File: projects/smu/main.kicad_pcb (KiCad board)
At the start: 4 copper layers, 94 parts, among them P301 CONN_01X15, P302 CONN_01X03, P401 CONN_01X12, P501 CONN_01X07, Q501 MMBT3904, Q502 MMBT3904, U301 LM741, U302 DG444, U303 LM741, U304 LM741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

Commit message: add nettie library etc
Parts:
- removed C411, C412: C, Capacitors_SMD:C_1206
- removed C501, C503, C506: 10uF, Capacitors_SMD:C_1206
- removed C502: 10p, Capacitors_SMD:C_1206
- removed C504, C505, C507, C508: 0.1uF, Capacitors_SMD:C_1206
- removed P301: CONN_01X15, Pin_Headers:Pin_Header_Straight_1x15
- removed P302: CONN_01X03, Pin_Headers:Pin_Header_Straight_1x03
- removed P401: CONN_01X12, Pin_Headers:Pin_Header_Straight_1x12
- removed P501: CONN_01X07, Pin_Headers:Pin_Header_Straight_1x07
- removed Q501, Q502: MMBT3904, TO_SOT_Packages_SMD:SOT-23
- removed R502: 1M, Resistors_SMD:R_1206
- removed R503: 10k, Resistors_SMD:R_1206
- removed R504: 1k, Resistors_ThroughHole:Resistor_TO-220_Vertical
- removed R505, R508: 10k, Resistors_ThroughHole:Resistor_TO-220_Vertical
- removed R506: 120, Resistors_ThroughHole:Resistor_TO-220_Vertical
- removed R507: 5.1k, Resistors_ThroughHole:Resistor_TO-220_Vertical
- removed R510: R, Resistors_SMD:R_1206
- removed RV501, RV502: 1k, Potentiometers:Potentiometer_Bourns_3296Y_3-8Zoll_Angular_ScrewUp
- removed U403, U406, U407, U501, U502: LM741, Housings_SOIC:SOIC-8_3.9x4.9mm_Pitch1.27mm
- removed U503: 2DW232, footprint:TO-5_Housing_2DW232_5Pin
- added P101: CONN_01X15, Pin_Headers:Pin_Header_Straight_1x15, F.Cu at (35.0, 64.0)
- added P102: CONN_01X34, Pin_Headers:Pin_Header_Straight_1x34, F.Cu at (-22.0, 1.00)
- added R307, R308: R, Resistors_SMD:R_1206, F.Cu at (0.00, 0.00)
- added W401, W402: NET-TIE, footprint:NET-TIE-0.3mm, F.Cu at (0.00, 0.00)
- U402, U404: value LM741 -> LM324; footprint Housings_SOIC:SOIC-8_3.9x4.9mm_Pitch1.27mm -> Housings_SOIC:SOIC-14_3.9x8.7mm_Pitch1.27mm
- U405: value LM741 -> DG444; footprint Housings_SOIC:SOIC-8_3.9x4.9mm_Pitch1.27mm -> Housings_SOIC:SOIC-16_3.9x9.9mm_Pitch1.27mm
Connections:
- R403 pad 1: REFGND -> AGND
- R416 pad 2: REF-CTL -> Net-(R416-Pad2)
- U401 pad 11: (no net) -> AGND
- U401 pad 18: REFGND -> AGND
- U401 pad 2: (no net) -> DAC_CS
- U401 pad 20: REFGND -> AGND
- U401 pad 29: REFGND -> AGND
- U401 pad 3: (no net) -> DAC_SLCK
- U401 pad 32: REFGND -> AGND
- U401 pad 4: (no net) -> DAC_SDI
- U401 pad 41: REFGND -> AGND
- U401 pad 43: REFGND -> AGND
- U401 pad 5: (no net) -> DAC_SDO
- U401 pad 6: (no net) -> DAC_LDAC
- U401 pad 7: (no net) -> DAC_RST
- U402 pad 2: Net-(R404-Pad1) -> AGND
- U402 pad 4: -VE -> +VE
- U402 pad 5: (no net) -> AGND
- U402 pad 6: Net-(R406-Pad1) -> AGND
- U402 pad 7: +VE -> (no net)
- U402 pad 8: (no net) -> Net-(R406-Pad1)
- U404 pad 1: (no net) -> Net-(D401-Pad2)
- U404 pad 4: -VE -> +VE
- U404 pad 5: (no net) -> Net-(R412-Pad1)
- U404 pad 6: Net-(D401-Pad2) -> OUT
- U404 pad 7: +VE -> Net-(D404-Pad1)
- U404 pad 8: (no net) -> Net-(D402-Pad2)
- U405 pad 1: (no net) -> REF_IN1
- U405 pad 2: OUT -> Net-(R416-Pad2)
- U405 pad 3: Net-(R412-Pad1) -> Net-(U405-Pad3)
- U405 pad 5: (no net) -> AGND
- U405 pad 6: Net-(D404-Pad1) -> AGND
- U405 pad 7: +VE -> Net-(R416-Pad2)
- U405 pad 8: (no net) -> REF_IN4
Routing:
- net REF: track 286.8 -> 98.1 mm
- net OUT: track 140.1 -> 0.00 mm, vias 2 -> 0
- net 3.3V: track 132.9 -> 7.72 mm, vias 3 -> 0
- net TRIGGER: track 118.4 -> 3.27 mm
- net H-GND: track 75.1 -> 0.00 mm
- net Net-(Q502-Pad2): track 71.0 -> 0.00 mm
- net REF-CTL: track 68.1 -> 0.00 mm, vias 1 -> 0
- net -VE: track 167.6 -> 100.2 mm, vias 17 -> 14
- net +VE: track 194.9 -> 128.1 mm, vias 21 -> 14
- net AGND: track 234.8 -> 176.9 mm, vias 33 -> 26
- net Net-(Q501-Pad2): track 48.4 -> 0.00 mm
- net I-FB: track 58.1 -> 15.2 mm
- net V-FB: track 53.0 -> 12.4 mm
- net Net-(R307-Pad1): track 35.4 -> 0.18 mm
- net Net-(C502-Pad1): track 33.0 -> 0.00 mm
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
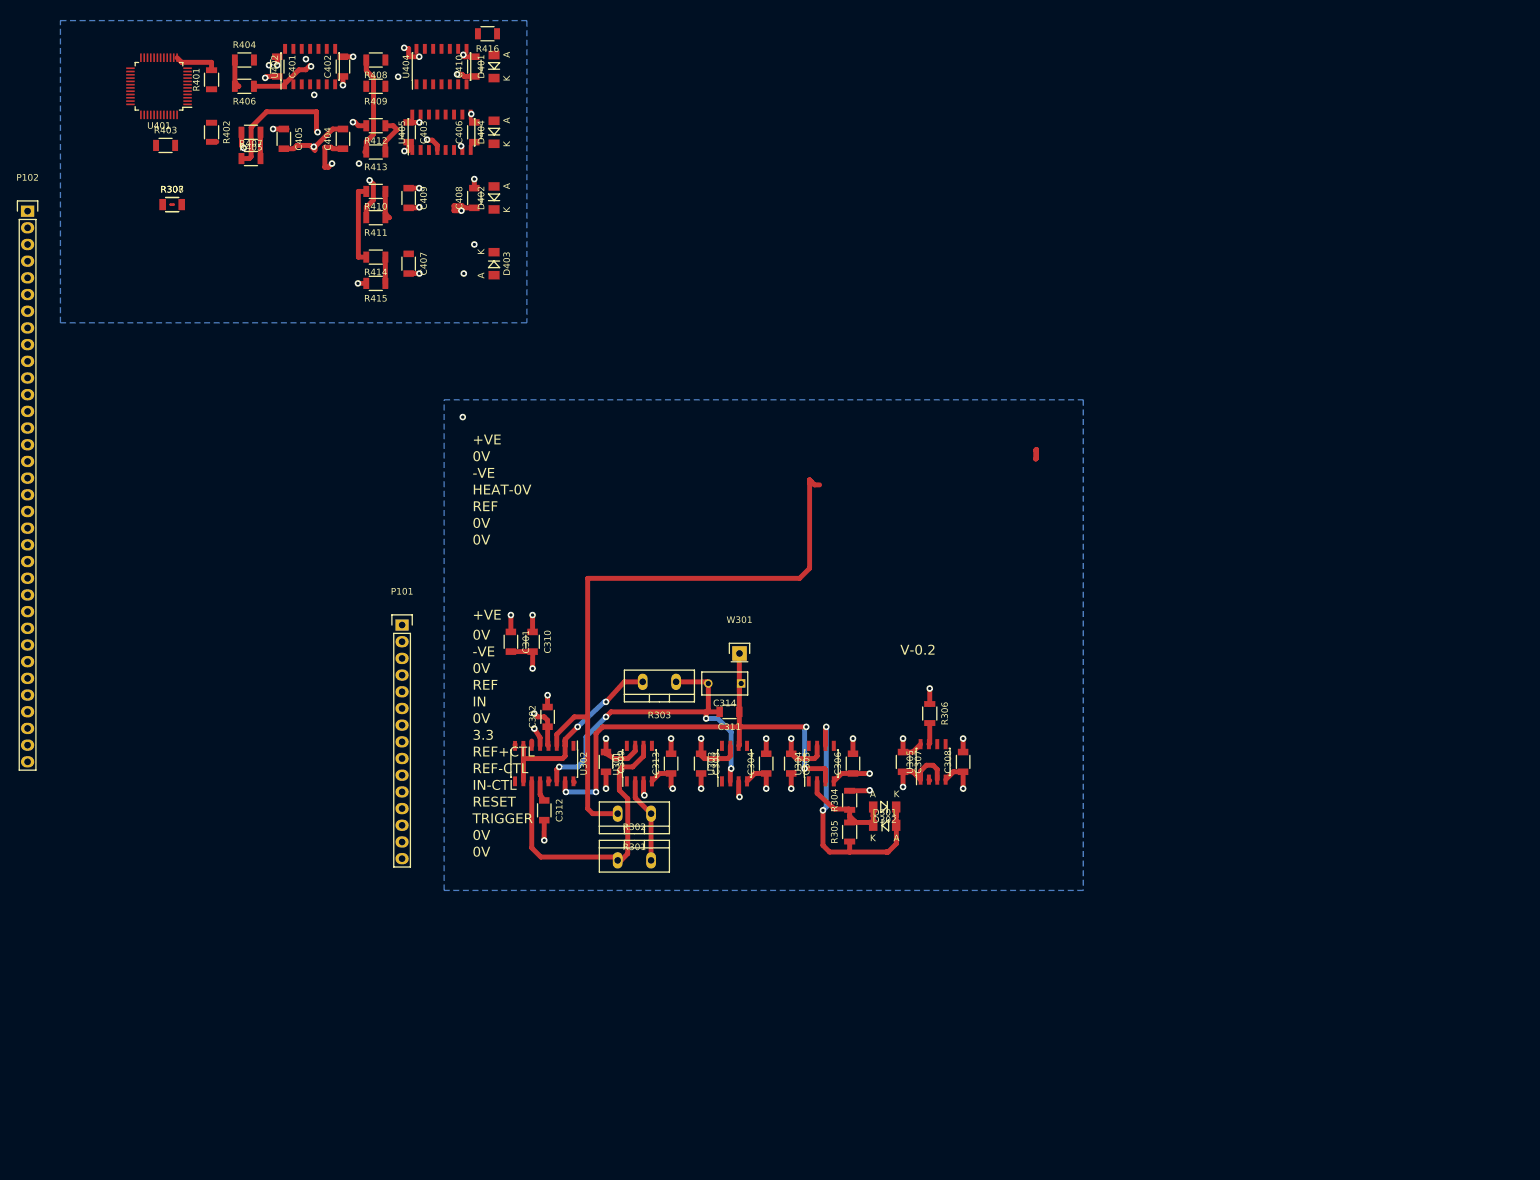
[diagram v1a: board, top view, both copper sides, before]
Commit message: change resistors to all 1206
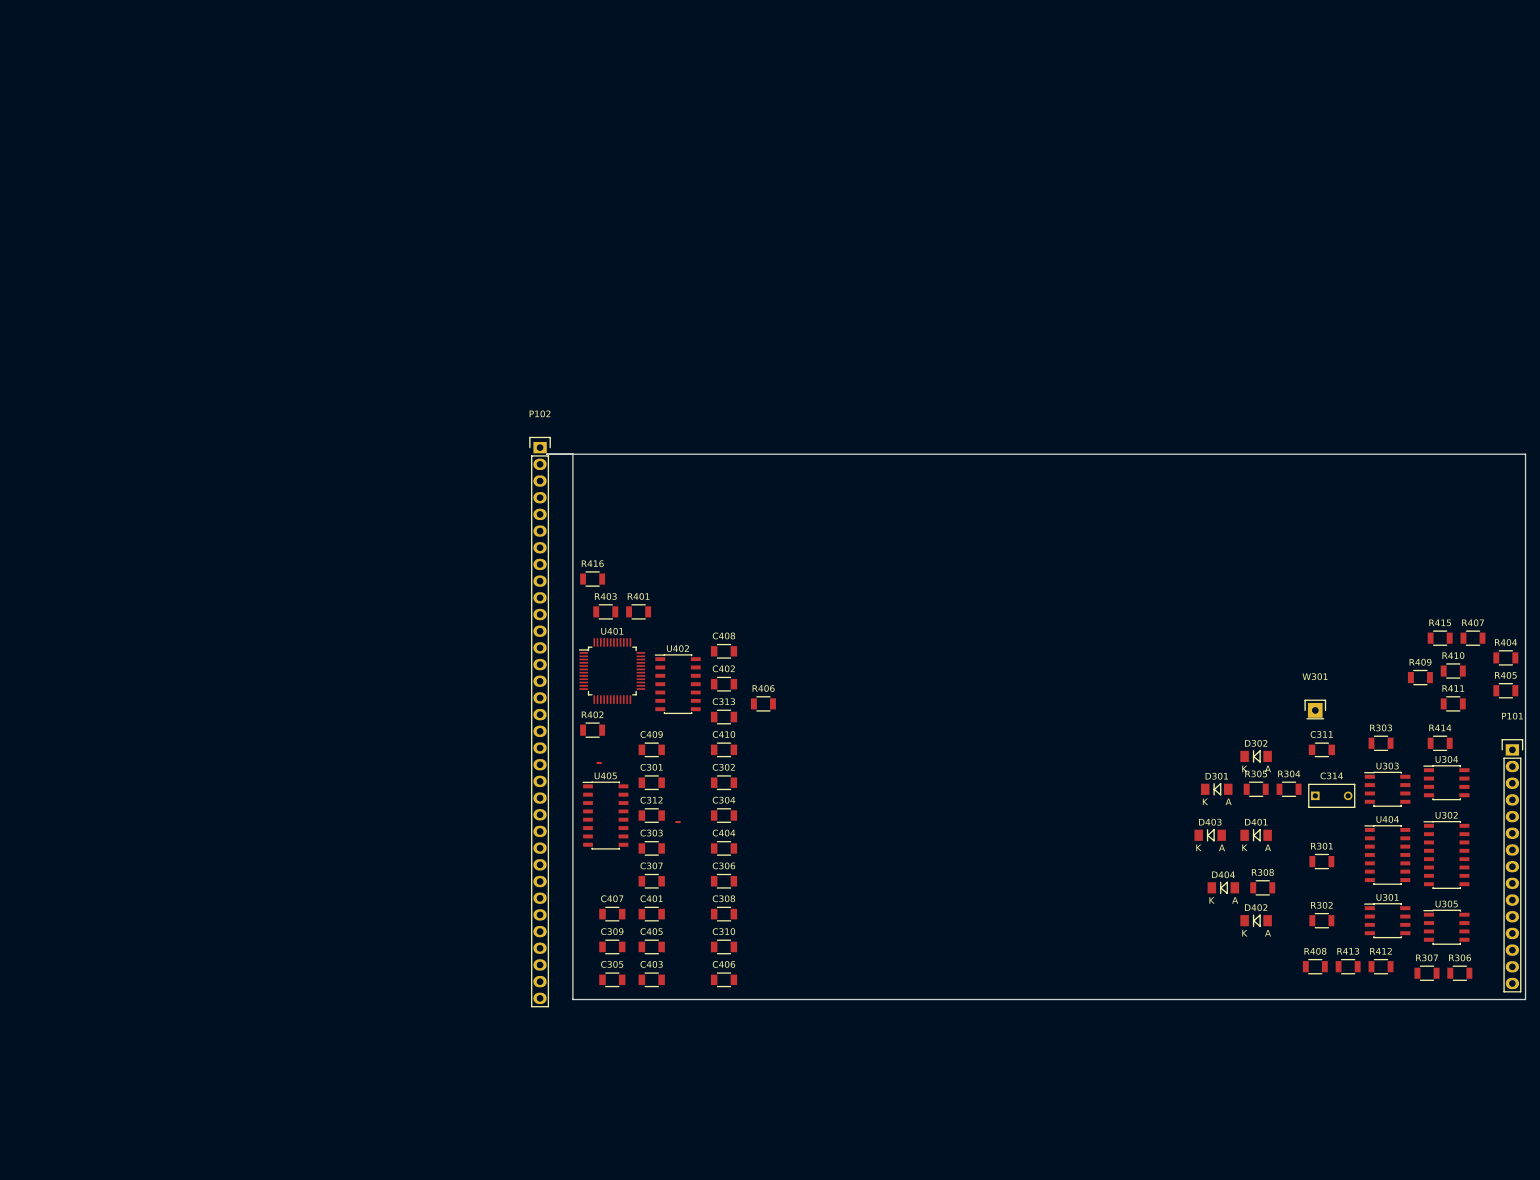
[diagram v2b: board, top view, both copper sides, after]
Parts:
- R301, R302: footprint Resistors_ThroughHole:Resistor_TO-220_Vertical -> Resistors_SMD:R_1206
- R303: value R -> 0R; footprint Resistors_ThroughHole:Resistor_TO-220_Vertical -> Resistors_SMD:R_1206
- R307, R308: value R -> 0R
- moved R307 224.0 mm to (191.0, 117.0)
- moved R404 212.5 mm to (203.0, 69.0)
- moved R405 209.1 mm to (203.0, 74.0), turned to 0 degrees
- moved R407 199.8 mm to (198.0, 66.0)
- moved R412 199.5 mm to (184.0, 116.0), turned to 0 degrees
- moved R408 198.7 mm to (174.0, 116.0), turned to 0 degrees
- moved R308 195.9 mm to (166.0, 104.0)
- moved R413 193.1 mm to (179.0, 116.0), turned to 0 degrees
- moved U404 187.4 mm to (185.0, 99.0), turned to 0 degrees
- moved R409 182.7 mm to (190.0, 72.0), turned to 0 degrees
- moved R411 179.9 mm to (195.0, 76.0), turned to 0 degrees
- moved R410 179.5 mm to (195.0, 71.0), turned to 0 degrees
- moved R414 178.1 mm to (193.0, 82.0), turned to 0 degrees
- moved R415 170.8 mm to (193.0, 66.0), turned to 0 degrees
- moved P101 170.1 mm to (204.0, 83.0)
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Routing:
- net AGND: track 176.9 -> 0.00 mm, vias 26 -> 0
- net +VE: track 128.1 -> 0.00 mm, vias 14 -> 0
- net -VE: track 100.2 -> 0.00 mm, vias 14 -> 0
- net REF: track 98.1 -> 0.00 mm
- net Net-(C311-Pad1): track 75.2 -> 0.00 mm, vias 4 -> 0
- net Net-(C311-Pad2): track 55.2 -> 0.00 mm, vias 4 -> 0
- net Net-(R407-Pad1): track 47.1 -> 0.00 mm, vias 2 -> 0
- net Net-(R302-Pad1): track 45.8 -> 0.00 mm
- net Net-(D301-Pad2): track 42.9 -> 0.00 mm, vias 2 -> 0
- net Net-(R303-Pad2): track 30.6 -> 0.00 mm, vias 2 -> 0
- net V-SET: track 30.1 -> 0.00 mm, vias 2 -> 0
- net Net-(R406-Pad1): track 23.4 -> 0.00 mm, vias 2 -> 0
- net Net-(D301-Pad1): track 18.8 -> 0.00 mm
- net I-FB: track 15.2 -> 0.00 mm
- net Net-(R301-Pad1): track 13.0 -> 0.00 mm
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- removed copper zone on In2.Cu, net +VE
- removed copper zone on B.Cu, net -VE
- removed copper zone on In1.Cu, net AGND
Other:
- board outline added: 149 x 83 mm
- net class Default: clearance 0.25 -> 0.2; trace_width 0.75 -> 0.25; via_dia 1 -> 0.6; via_drill 0.5 -> 0.4
- net class power removed
- rule trace_clearance: 0.25 -> 0.2
- board text removed: "+VE"
- board text removed: "-VE"
- board text removed: "0V"
- board text removed: "3.3"
- board text removed: "HEAT-0V"
- board text removed: "IN"
- board text removed: "IN-CTL"
- board text removed: "REF"
- board text removed: "REF+CTL"
- board text removed: "REF-CTL"
- board text removed: "RESET"
- board text removed: "TRIGGER"
- board text removed: "V-0.2"

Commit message: do edges again
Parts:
- P102: value CONN_01X34 -> CONN_01X28; footprint Pin_Headers:Pin_Header_Straight_1x34 -> Pin_Headers:Pin_Header_Straight_1x28
- moved P102 14.0 mm to (56.0, 51.0)
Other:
- board size 149 x 83 mm -> 100 x 100 mm

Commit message: ok somewhat laid out
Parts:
- added R417: 10k, Resistors_SMD:R_1206, F.Cu at (93.0, 90.5)
- moved R413 105.8 mm to (92.5, 55.0)
- moved P101 100.1 mm to (107.5, 109.5)
- moved R412 98.7 mm to (92.5, 79.0)
- moved R408 97.8 mm to (97.5, 55.0)
- moved R404 96.4 mm to (107.0, 77.5)
- moved R405 92.8 mm to (110.5, 66.5)
- moved U404 91.9 mm to (97.5, 71.0)
- moved R410 89.6 mm to (105.5, 67.5)
- moved R414 89.5 mm to (104.0, 72.5)
- moved R409 89.1 mm to (101.5, 82.0)
- moved R407 88.8 mm to (109.5, 58.5)
- moved R411 86.1 mm to (109.0, 72.5)
- moved R415 85.9 mm to (108.0, 53.5)
- moved D401 83.6 mm to (89.5, 60.0)
- moved D403 82.7 mm to (83.5, 60.0)
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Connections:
- P102 pad 25: REF_IN3 -> (no net)
- P102 pad 26: REF_IN4 -> (no net)
- U405 pad 16: REF_IN3 -> Net-(R417-Pad1)
- U405 pad 8: REF_IN4 -> Net-(R417-Pad1)

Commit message: ok routed
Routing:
- net AGND: track 0.00 -> 418.5 mm, vias 0 -> 10
- net -VE: track 0.00 -> 321.1 mm, vias 0 -> 4
- net +VE: track 0.00 -> 286.2 mm, vias 0 -> 5
- net 3.3V: track 0.00 -> 135.4 mm, vias 0 -> 3
- net REF: track 0.00 -> 134.9 mm, vias 0 -> 3
- net OUT: track 0.00 -> 102.7 mm, vias 0 -> 1
- net Net-(C311-Pad1): track 0.00 -> 95.3 mm, vias 0 -> 2
- net V-SET: track 0.00 -> 72.2 mm, vias 0 -> 2
- net I-SET: track 0.00 -> 63.5 mm, vias 0 -> 2
- net V-FB: track 0.00 -> 59.9 mm
- net Net-(C311-Pad2): track 0.00 -> 53.2 mm, vias 0 -> 2
- net Net-(R303-Pad2): track 0.00 -> 50.2 mm
- net RESET: track 0.00 -> 49.5 mm
- net REF_PLUS_CTL: track 0.00 -> 47.6 mm
- net Net-(D301-Pad2): track 0.00 -> 46.2 mm
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
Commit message: update
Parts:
- moved C409 58.6 mm to (91.0, 80.5), turned to 270 degrees
- moved C305 55.8 mm to (122.0, 100.5)
- moved C301 50.5 mm to (122.0, 96.5)
- moved C309 49.2 mm to (122.0, 105.0)
- moved R406 28.3 mm to (85.0, 56.5), turned to 0 degrees
- moved R407 24.5 mm to (85.0, 59.5)
- moved D403 23.7 mm to (104.5, 71.0), turned to 180 degrees
- moved R415 23.0 mm to (98.5, 74.5)
- moved R404 21.6 mm to (93.0, 61.0)
- moved C312 21.1 mm to (129.0, 96.5)
- moved D404 19.9 mm to (104.5, 74.5)
- moved R405 19.9 mm to (93.0, 57.0), turned to 180 degrees
- moved D402 19.2 mm to (104.5, 68.0)
- moved R409 17.3 mm to (98.5, 65.0)
- moved R413 17.1 mm to (98.5, 71.0)
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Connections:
- D402 pad 1: OUT -> Net-(D402-Pad1)
- D402 pad 2: Net-(D402-Pad2) -> OUT
- D403 pad 1: Net-(D403-Pad1) -> OUT
- D403 pad 2: OUT -> Net-(D403-Pad2)
- R405 pad 2: V-SET -> Net-(R404-Pad1)
- R406 pad 2: Net-(R404-Pad1) -> V-SET
- R407 pad 2: Net-(R405-Pad1) -> Net-(R406-Pad1)
- R410 pad 2: V-FB -> Net-(R405-Pad1)
- R411 pad 2: V-SET -> I-FB
- R412 pad 2: Net-(R406-Pad1) -> V-FB
- R413 pad 2: I-FB -> V-SET
- U402 pad 13: Net-(R405-Pad1) -> Net-(R406-Pad1)
- U402 pad 8: Net-(R406-Pad1) -> Net-(R405-Pad1)
- U404 pad 10: Net-(R410-Pad1) -> Net-(R412-Pad1)
- U404 pad 14: Net-(D403-Pad1) -> Net-(D404-Pad1)
- U404 pad 5: Net-(R412-Pad1) -> Net-(R410-Pad1)
- U404 pad 7: Net-(D404-Pad1) -> Net-(D402-Pad1)
- U404 pad 8: Net-(D402-Pad2) -> Net-(D403-Pad2)
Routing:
- net AGND: track 418.5 -> 0.00 mm, vias 10 -> 0
- net -VE: track 321.1 -> 0.00 mm, vias 4 -> 0
- net +VE: track 286.2 -> 0.00 mm, vias 5 -> 0
- net 3.3V: track 135.4 -> 0.00 mm, vias 3 -> 0
- net REF: track 134.9 -> 0.00 mm, vias 3 -> 0
- net OUT: track 102.7 -> 0.00 mm, vias 1 -> 0
- net Net-(C311-Pad1): track 95.3 -> 0.00 mm, vias 2 -> 0
- net V-SET: track 72.2 -> 0.00 mm, vias 2 -> 0
- net I-SET: track 63.5 -> 0.00 mm, vias 2 -> 0
- net V-FB: track 59.9 -> 0.00 mm
- net Net-(C311-Pad2): track 53.2 -> 0.00 mm, vias 2 -> 0
- net Net-(R303-Pad2): track 50.2 -> 0.00 mm
- net RESET: track 49.5 -> 0.00 mm
- net REF_PLUS_CTL: track 47.6 -> 0.00 mm
- net Net-(D301-Pad2): track 46.2 -> 0.00 mm
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- added copper zone on In2.Cu, net +VE
- added copper zone on B.Cu, net -VE
- added copper zone on In1.Cu, net AGND
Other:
- net class Default: clearance 0.2 -> 0.3; trace_width 0.25 -> 0.6; via_dia 0.6 -> 0.8
- net class dac added: clearance 0.2, trace_width 0.2, via_dia 0.6, via_drill 0.4
- rule trace_clearance: 0.2 -> 0.3
